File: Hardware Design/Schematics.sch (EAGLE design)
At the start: 1 part

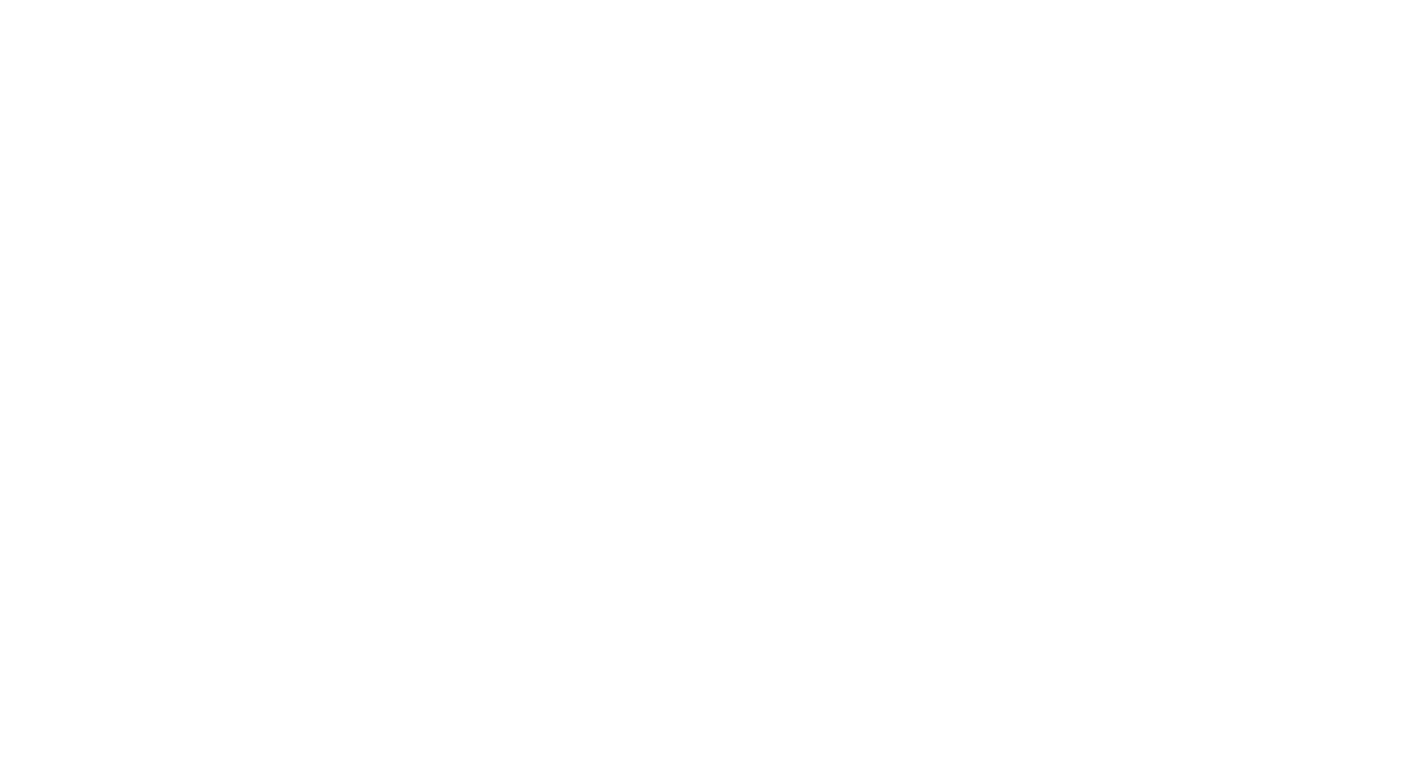
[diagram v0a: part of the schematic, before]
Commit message: ...Now Calculates Average Force
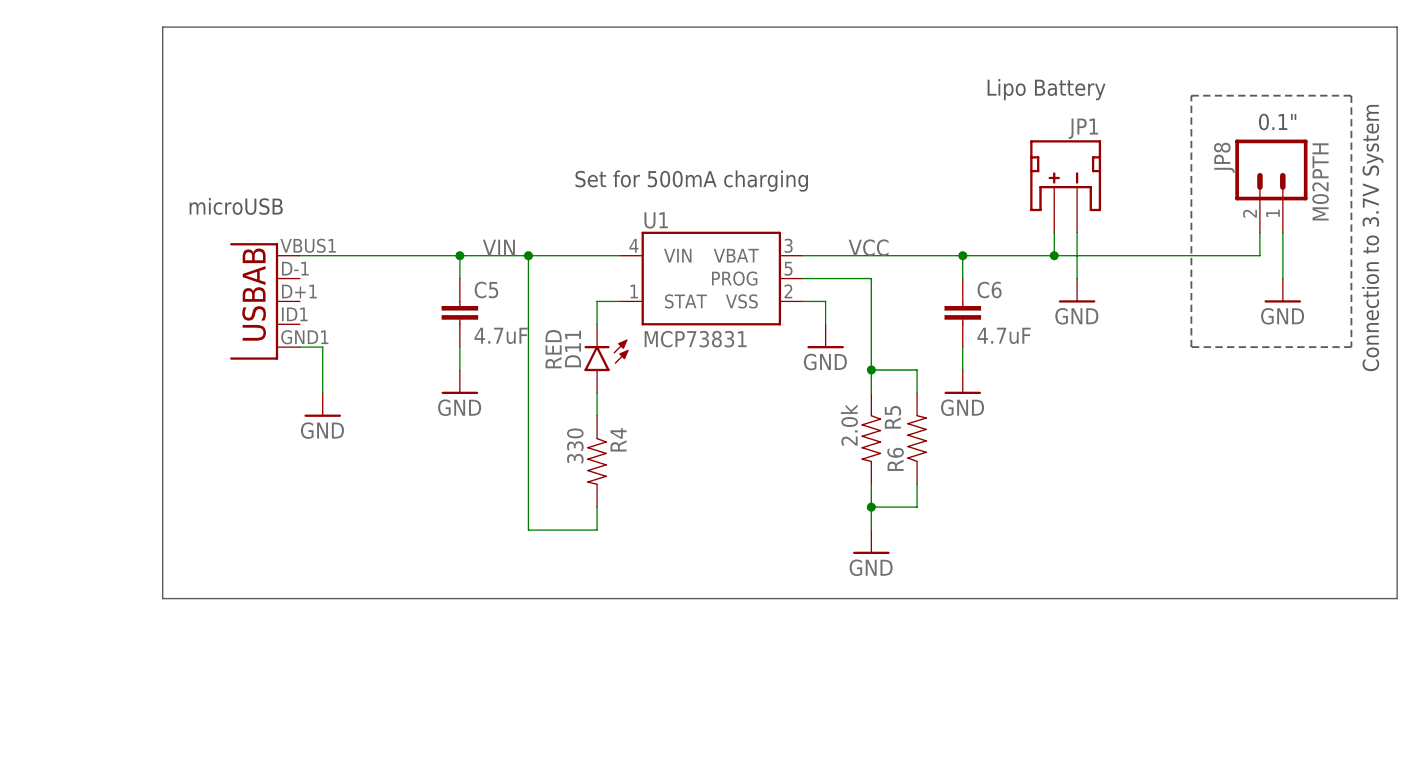
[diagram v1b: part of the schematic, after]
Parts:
- added C5, C6: 4.7uF, SparkFun-Capacitors:4.7UF-6.3V-10%(0603)0603
- added D11: RED, SparkFun-LED:LED-RED0603
- added JP1: JST, SparkFun-Connectors:JST_2MM_MALE
- added JP8: M02PTH, SparkFun-Connectors:M02PTH
- added JP9: Micro USB, SparkFun-Connectors:USB-ABCONN-11794
- added R4: 330, SparkFun-Resistors:330OHM1/10W1%(0603)
- added R5: 2.0k, SparkFun-Resistors:2.0KOHM1/10W5%(0603)
- added R6: (no value), SparkFun-Resistors:RESISTORPTH-1/4W-VERT-KIT
- added U1: MCP73831, SparkFun-PowerIC:MCP73831
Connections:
- new net GND: C5.2, C6.2, JP1.-, JP8.1, JP9.GND, R5.2, R6.1, U1.VSS
- new net N$8: D11.A, R4.1
- new net PROG: R5.1, R6.2, U1.PROG
- new net STAT: D11.C, U1.STAT
- new net VCC: C6.1, JP1.+, JP8.2, U1.VBAT
- new net VIN: C5.1, JP9.VBUS, R4.2, U1.VIN
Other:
- note added: "0.1""
- note added: "Connection to 3.7V System"
- note added: "Lipo Battery"
- note added: "Set for 500mA charging"
- note added: "microUSB"

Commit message: Hardware design update
hardware design updated
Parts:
- added C1, C2, C3: 0.1uF, SparkFun-Capacitors:0.1UF-25V(+80/-20%)(0603)
- added C10, C9: 6pF, nrf52832-breakout-temp:6PF-0402-50V-0.5%
- added C11, C22: DNP, SparkFun-Passives:CAP0402
- added C12: 1.0uF, SparkFun-Capacitors:1.0UF-0402-16V-10%
- added C13, C14: 15pF, SparkFun-Capacitors:15PF-0402-50V-5%
- added C15, C16, C8: 0.1uF, SparkFun-Capacitors:0.1UF-0402-16V-10%
- added C17: 4.7uF, SparkFun-Capacitors:4.7UF0603
- added C18: 0.8pF, nrf52832-breakout-temp:0.8PF-0402-50V-0.1PF
- added C19: 100pF, nrf52832-breakout-temp:100PF-0402-50V-5%
- added C20: 1.0uF, SparkFun-Capacitors:1.0UF-0603-16V-10%
- added C21: 2.2uF, SparkFun-Capacitors:2.2UF-0603-10V-20%
- added C23, C24: 180pF, nrf52832-breakout-temp:180PF-0603-50V-5%
- added C25, C26: 10uF, SparkFun-Capacitors:10UF50V20%(1210)
- added C27, C28, C29, C30, C31: 0.1uF, SparkFun-Capacitors:0.1UF-25V-5%(0603)
- added C4: 10nF, SparkFun-Capacitors:10NF/10000PF-50V-10%(0603)
- added C7: 10uF, SparkFun-Capacitors:10UF-6.3V-20%(0603)
- added D1: RED, SparkFun-LED:LED-RED0603
- added D2: BLUE, SparkFun-LED:LED-BLUE0603
- added E1: ANT, SparkFun-RF:ANTENNA-GROUNDEDTRACE-15.2MM
- added J1: (no value), SparkFun-Connectors:ARDUINO_SERIAL_PROGRAMPTH
- added J2: (no value), SparkFun-Connectors:CONN_02PTH
- added J3, J4: (no value), SparkFun-Connectors:CONN_17
- added J5: CORTEX_DEBUGPTH, SparkFun-Connectors:CORTEX_DEBUGPTH
- added J6, JP13: (no value), SparkFun-Connectors:M05PTH
- added JP10: NFC2, SparkFun-Jumpers:JUMPER-SMT_2_NO_SILK
- added JP11: PWR-LED, SparkFun-Jumpers:JUMPER-PAD-2-NC_BY_TRACE
- added JP12: (no value), SparkFun-Connectors:M02PTH
- added JP2: (no value), SparkFun-Connectors:I2C_STANDARD_NO_SILK
- added JP3: M09NO_SILK, SparkFun-Connectors:M09NO_SILK
- added JP4: XL1, SparkFun-Jumpers:JUMPER-PAD-2-NC_BY_TRACE
- added JP5: XL2, SparkFun-Jumpers:JUMPER-PAD-2-NC_BY_TRACE
- added JP6: VDD-EN, SparkFun-Jumpers:JUMPER-SMT_2_NC_TRACE_SILK
- added JP7: NFC1, SparkFun-Jumpers:JUMPER-SMT_2_NO_SILK
- added L1: 3.9nH, nrf52832-breakout-temp:INDUCTOR-0402-3.9NH
- added L2: 3.3uH, SparkFun-Passives:INDUCTOR0805-IND
- added Q1: MMBT4403, SparkFun-DiscreteSemi:TRANSISTOR_PNPMMBT4403
- added R1, R16, R2, R3, R7, R8, R9: 10K, SparkFun-Resistors:10KOHM-1/10W-1%(0603)0603
- added R10, R11: 1k, SparkFun-Resistors:1KOHM-0603-1/10W-1%
- added R12, R13: 100, SparkFun-Resistors:100OHM-1/10W-1%(0603)
- added R14: 8.2K, SparkFun-Resistors:8.2KOHM-1/10W-5%(0603)
- added R15: 20k, SparkFun-Resistors:20KOHM1/10W1%(0603)
- added SJ1, SJ2, SJ3: (no value), SparkFun-Passives:JUMPER-PAD-3-NC_BY_TRACE
- added SJ4: JUMPER-PAD-2-NC_BY_TRACE, SparkFun-Passives:JUMPER-PAD-2-NC_BY_TRACE
- added SW1, SW2: (no value), SparkFun-Electromechanical:SWITCH_SPST_4_PINRECT
- added TP1, TP2: TEST-POINT3X4, SparkFun-Connectors:TEST-POINT3X4
- added U2: LSM9DS1, LSM9DS1_temp:LSM9DS1
- added U3: NRF52832, nrf52832-breakout-temp:NRF52832
- added U4: AP2112K-3.3V, SparkFun-PowerIC:V_REG_AP2112K-3.3V
- added U5: HX711, Testing:HX711HX711
- added Y1: 32MHz, nrf52832-breakout-temp:CRYSTAL-32MHZ-SMD-2.0X1.6MM
- added Y2: 32.768kHz, SparkFun-Clocks:CRYSTAL-32.768KHZSMD-3.2X1.5
- JP8: value M02PTH -> (none)
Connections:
- new net !RESET!: J3.4, J5.!RESET, SW1.1, SW1.2, U3.P0.21/RESET
- new net A+: JP13.2, R13.1
- new net A-: JP13.3, R12.1
- new net ANT: C18.2, L1.2, U3.ANT
- new net AVDD: C26.1, C30.1, JP13.5, L2.1
- new net B+: JP12.1, U5.INB+
- new net B-: JP12.2, U5.INB-
- new net C1: C1.1, U2.C1
- new net CAP: C4.1, U2.CAP
- new net CS_A/G: JP3.3, R1.1, U2.CS_A/G
- new net CS_A/G_PU: R1.2, SJ1.3
- new net CS_M: JP3.4, R2.1, U2.CS_M
- new net CS_M_PU: R2.2, SJ1.1
- new net DAT: J6.3, U5.DOUT
- new net DCC: U3.DCC
- new net DEC1: C8.2, U3.DEC1
- new net DEC2: C11.2, U3.DEC2
- new net DEC3: C19.2, U3.DEC3
- new net DEC4: C12.2, U3.DEC4
- new net DEN_A/G: JP3.9, U2.DEN_A/G
- new net DRDY_M: JP3.5, U2.DRDY_M
- new net INT1_A/G: JP3.7, U2.INT1_A/G
- new net INT2_A/G: JP3.8, U2.INT2_A/G
- new net INT_M: JP3.6, U2.INT_M
- new net N$1: JP11.2, R11.1
- new net N$10: C27.1, R12.2, U5.INA-
- new net N$11: C22.1, E1.SIGNAL, L1.1
- new net N$12: D1.C, R11.2
- new net N$13: C27.2, R13.2, U5.INA+
- new net N$14: J1.VCC, JP6.1
- new net N$15: D2.A, R10.1
- new net N$2: Q1.B, U5.BASE
- new net N$3: C13.2, JP4.1, Y2.2
- new net N$4: C14.2, JP5.1, Y2.1
- new net N$5: L2.2, Q1.C, R15.2, U5.AVDD
- new net N$6: R14.2, R15.1, U5.VFB
- new net N$7: C29.2, U5.VBG
- new net N$9: R16.1, SJ4.2, U5.RATE
- new net NC: U3.NC
- new net NFC1: C23.1, JP7.1
- new net NFC2: C24.1, JP10.1
- new net P00: J4.4, JP4.2, U3.P0.00/XL1
- new net P01: J4.5, JP5.2, U3.P0.01/XL2
- new net P02: J4.6, U3.P0.02/AIN0
- new net P03: J4.7, U3.P0.03/AIN1
- new net P04: J4.8, U3.P0.04/AIN2
- new net P05: J4.9, U3.P0.05/AIN3
- new net P06: SW2.1, SW2.2, U3.P0.06
- new net P07: D2.C, U3.P0.07
- new net P08: J4.10, U3.P0.08
- new net P09: J2.2, J4.11, JP7.2, U3.P0.09/NFC1
- new net P10: J2.1, J4.12, JP10.2, U3.P0.10/NFC2
- new net P11: J4.13, U3.P0.11
- new net P12: J4.14, U3.P0.12
- new net P13: J4.15, U3.P0.13
- new net P14: J4.16, U3.P0.14
- new net P15: J4.17, U3.P0.15
- new net P16: J3.17, U3.P0.16
- new net P17: J3.16, U3.P0.17
- new net P18: J3.15, J5.SWO/TDO, U3.P0.18
- new net P19: J3.14, U3.P0.19
- new net P20: J3.13, U3.P0.20
- new net P22: J3.12, U3.P0.22
- new net P23: J3.11, U3.P0.23
- new net P24: J3.10, U3.P0.24
- new net P25: J3.9, U3.P0.25
- new net P26: J1.TXO, U3.P0.26
- new net P27: J1.RXI, U3.P0.27
- new net P28: J3.8, U3.P0.28/AIN4
- new net P29: J3.7, U3.P0.29/AIN5
- new net P30: J3.6, U3.P0.30/AIN6
- new net P31: J3.5, U3.P0.31/AIN7
- new net SCK: J6.4, U5.PD_SCK
- new net SCL: JP2.4, R9.1, U2.SCL/SPC
- new net SCL_PU: R9.2, SJ3.3
- new net SDA: JP2.3, R8.1, U2.SDA/SDI/SDO
- new net SDA_PU: R8.2, SJ3.1
- new net SDO_A/G: JP3.1, R3.1, U2.SDO_A/G
- new net SDO_A/G_PU: R3.2, SJ2.3
- new net SDO_M: JP3.2, R7.1, U2.SDO_M
- new net SDO_M_PU: R7.2, SJ2.1
- new net SWDCLK: J5.SWDCLK/TCK, TP2.1, U3.SWDCLK
- new net SWDIO: J5.SWDIO/TMS, TP1.1, U3.SWDIO
- new net VDD: C15.1, C16.1, C17.1, C2.1, C21.1, C3.1, C31.1, C7.1, D1.A, J3.3, J4.3, J5.VCC, J6.1, JP2.2, JP6.2, R10.2, SJ1.2, SJ2.2, SJ3.2, U2.VDD, U2.VDDIO, U3.VDD, U4.OUT, U5.DVDD
- new net XC1: C9.2, U3.XC1(32MHZ), Y1.2
- new net XC2: C10.1, U3.XC2(32MHZ), Y1.1
- net GND: now also C1.2, C10.2, C11.1, C12.1, C13.1, C14.1, C15.2, C16.2, C17.2, C18.1, C19.1, C2.2, C20.2, C21.2, C22.2, C23.2, C24.2, C25.2, C26.2, C28.2, C29.1, C3.2, C30.2, C31.2, C4.2, C7.2, C8.1, C9.1, E1.GND, J1.GND, J3.1, J4.1, J5.GND@3, J5.GND@5, J5.GNDDTCT, J6.5, JP11.1, JP13.1, JP13.4, JP2.1, R14.1, SJ4.1, SW1.3, SW1.4, SW2.3, SW2.4, U2.GND, U2.RES, U3.VSS, U4.GND, U5.AGND, U5.XI
- net VCC: now also C25.1, C28.1, J6.2, Q1.E, R16.2, U5.VSUP
- net VIN: now also C20.1, J3.2, J4.2, U4.EN, U4.IN
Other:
- note added: "0 1"
- note added: "0x1C 0x1E"
- note added: "0x6A 0x6B"
- note added: "32.768kHz Crystal (RTC)"
- note added: "A+"
- note added: "A-"
- note added: "AG Addr."
- note added: "AVDD = VBG(R1+R2)/R1"
- note added: "Black"
- note added: "Buttons"
- note added: "Close JP2 & JP3 if you're attaching an NFC antenna."
- note added: "Common Load Cell Colors:"
- note added: "Cortex Debug Connector"
- note added: "Ctune (C7/8) = 2/((2*PI*13.56MHz)^2*La) La is inductance of NFC antenna La=1.5uH, Ctune=~180pF La=2.0uH, Ctune=~130pF"
- note added: "Cut JP6 to disable the power LED."
- note added: "Default: Closed - Data rate set to 10SPS"
- note added: "E+"
- note added: "E-"
- note added: "Green or Blue"
- note added: "Headers"
- note added: "I2C Address Table"
- note added: "IO: 2.7-5.5V"
- note added: "JP4 and JP5 enable the RTC on pins 00 and 01."
- note added: "Jumpers"
- note added: "LEDs"
- note added: "LSM9DS1"
- note added: "M Addr."
- note added: "NFC Antenna Interface"
- note added: "NFC Tuning Caps"
- note added: "Open JP1 to disable powering the nRF52832 via a 3.3V FTDI Basic"
- note added: "Open jumper to set to 80SPS Increases noise per read"
- note added: "Pin 13"
- note added: "Pin 36"
- note added: "Pin 48"
- note added: "Pin/Supply Headers"
- note added: "Red"
- note added: "Regulator Input Voltage !3.3 - 6V DC!"
- note added: "SDOM/AG"
- note added: "SJ1 pulls up the chip-select (CS) pins. Closed: Sets LSM9DS1 to I2C mode. Open: Allows for CS control in SPI mode."
- note added: "SJ2 pulls up the serial data out (SDO) pins. Closed: Sets I2C addresses in I2C mode. Open: Floats SDO pins - can be used to set I2C address, or be used for SPI control"
- note added: "SJ3 pulls up the SCL and SDA pins. Closed: Adds 10k pull-ups to I2C lines. Open: Removes 10k pull-ups. SPI mode or external I2C pull-ups can be used."
- note added: "Serial Program/Debug"
- note added: "Set the SDO_AG and SDO_M to set the accel/gryo and mag I2C addresses:"
- note added: "Shield"
- note added: "Supply Decoupling"
- note added: "VBG = 1.25V"
- note added: "VCC vs VDD: VCC is the main supply voltage, while VDD sets the digital logic voltage reference and should be connected to microcontroller supply voltage, or shorted to VCC."
- note added: "VCC: 2.7-5.5V"
- note added: "VDD Range: 1.9-3.6V"
- note added: "VDD: 2.7-5.5V"
- note added: "Voltage Regulator"
- note added: "White"
- note added: "Yellow"
- note added: "nRF52832"
- note added: "nRF52832 Supply Range !1.7 - 3.6V DC!"
